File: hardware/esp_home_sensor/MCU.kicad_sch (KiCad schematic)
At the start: 9 parts, among them SW1 SW_Push, SW2 SW_Push, U6 ESP32-C6-MINI-1

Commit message: busses, display connector, footprint lib
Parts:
- added C15, C16: C, symbol Device:C
- added SW3: SW_Push, symbol Switch:SW_Push
- D3: footprint LED_SMD:LED_WS2812B_PLCC4_5.0x5.0mm_P3.2mm -> LED_SMD:LED_WS2812B-2020_PLCC4_2.0x2.0mm
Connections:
- net 3V3_EN: now also U6.13 (IO1); no longer U6.26 (IO20)
- net ADC_BAT: now also U6.5 (IO2); no longer U6.28 (IO22)
- net BOOT: now also C16.1
- net GND: now also C15.2, C16.2, SW3.1
- net LED_DATA: now also U6.12 (IO0); no longer U6.27 (IO21)
- net USER_SW: now also C15.1, SW3.2
- net I2C.SDA: now reaches U6.19 (IO14)
- net I2C.SCL: now reaches U6.20 (IO15)
- net DISP_IF.RST: now reaches U6.29 (IO23)
- net SCL renamed DISP_IF.MOSI
- net SDA renamed DISP_IF.CLK
- net USB_N renamed USB.USB_N
- net USB_P renamed USB.USB_P
- new net DISP_IF.BUSY: U6.28 (IO22)
- new net DISP_IF.CS: U6.26 (IO20)
- new net DISP_IF.DC: U6.27 (IO21)
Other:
- moved on the sheet: SW2

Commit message: footprint assignment, buck
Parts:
- C12, C13: value C -> 4.7u; footprint (none) -> Capacitor_SMD:C_0402_1005Metric
- C15, C16: value C -> 100n; footprint (none) -> Capacitor_SMD:C_0402_1005Metric
- C9: value C -> 1u; footprint (none) -> Capacitor_SMD:C_0402_1005Metric
- R12: value R -> 100k; footprint (none) -> Resistor_SMD:R_0402_1005Metric
- SW1, SW2, SW3: Mfr. No. (none) -> B3FS-1010P
- U6: Mfr. No. (none) -> ESP32-C6-MINI-1U-N4
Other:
- moved on the sheet: C15, C16, C9, R12, SW1, SW2, SW3

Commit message: minor update
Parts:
- JP2: footprint (none) -> Jumper:SolderJumper-3_P1.3mm_Bridged12_Pad1.0x1.5mm
- SW1, SW2, SW3: footprint (none) -> Button_Switch_SMD:SW_SPST_Omron_B3FS-101xP
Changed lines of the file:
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@@
 			)
 		)
-		(property "Footprint" ""
+		(property "Footprint" "Jumper:SolderJumper-3_P1.3mm_Bridged12_Pad1.0x1.5mm"
 			(at 232.41 95.25 0)
 			(hide yes)
@@
 			)
 		)
-		(property "Footprint" ""
+		(property "Footprint" "Button_Switch_SMD:SW_SPST_Omron_B3FS-101xP"
 			(at 99.06 119.38 0)
 			(hide yes)
@@
 			)
 		)
-		(property "Footprint" ""
+		(property "Footprint" "Button_Switch_SMD:SW_SPST_Omron_B3FS-101xP"
 			(at 71.12 90.17 0)
 			(hide yes)
@@
 			)
 		)
-		(property "Footprint" ""
+		(property "Footprint" "Button_Switch_SMD:SW_SPST_Omron_B3FS-101xP"
 			(at 71.12 119.38 0)
 			(hide yes)

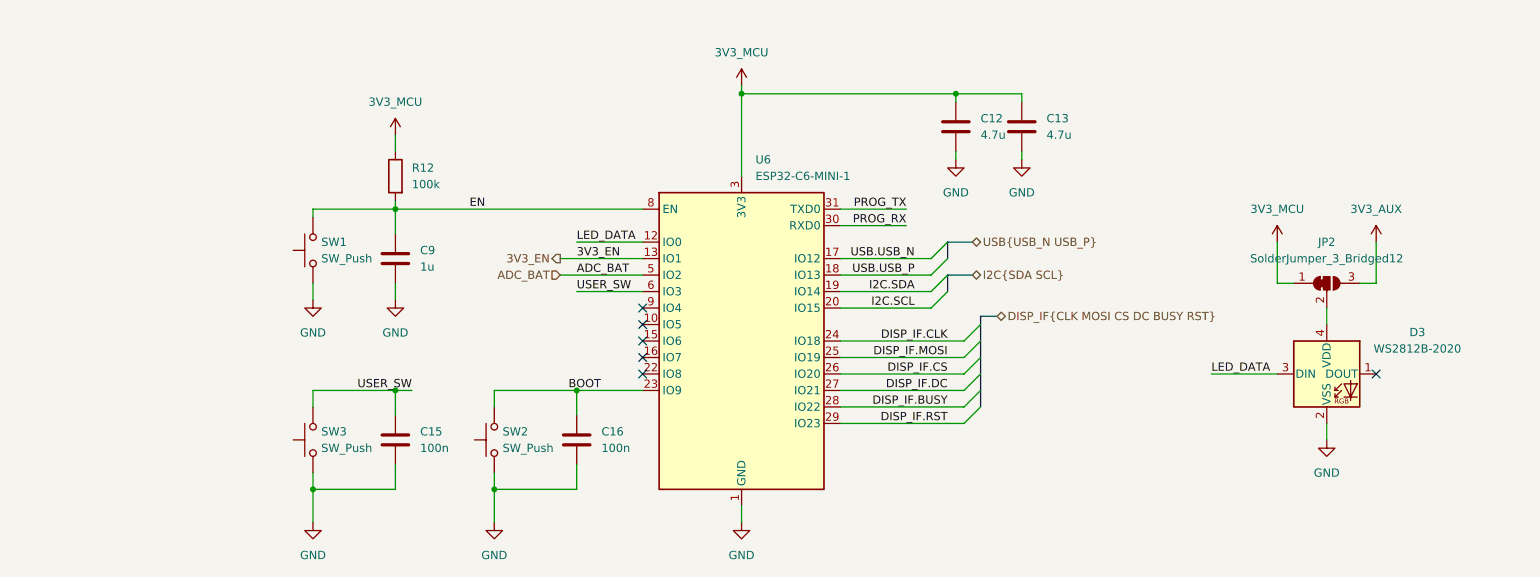
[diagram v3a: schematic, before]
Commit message: initial layout, power routing
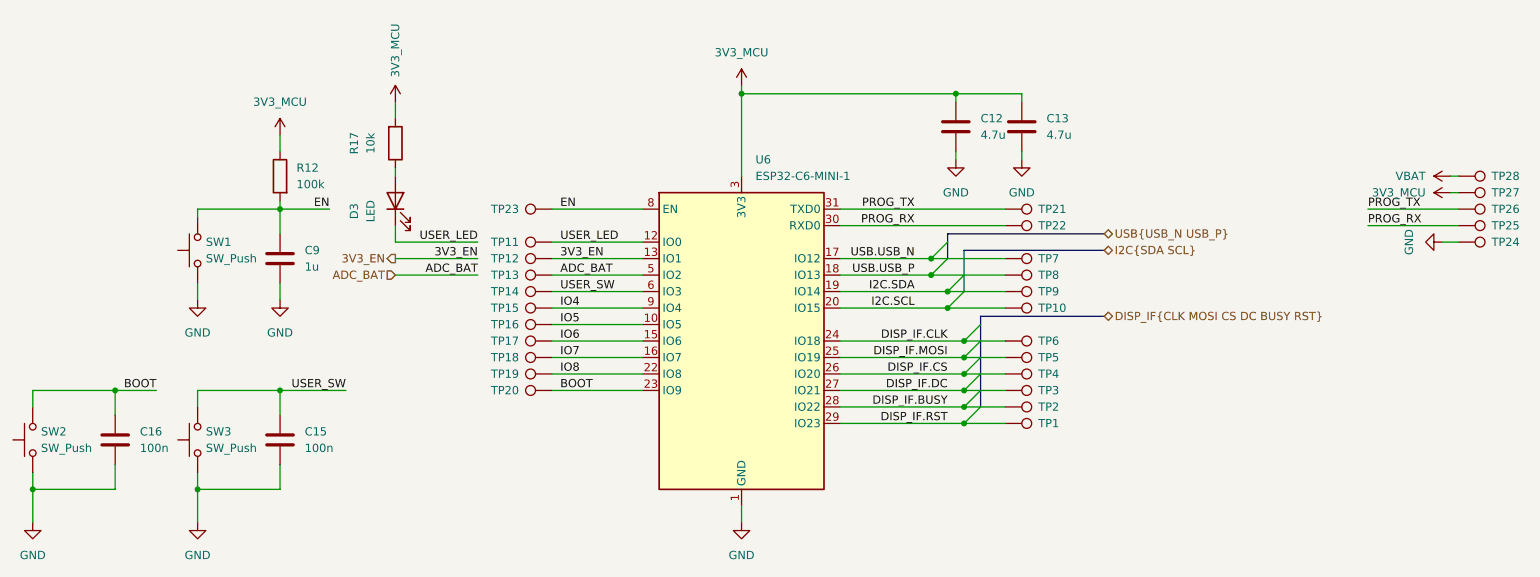
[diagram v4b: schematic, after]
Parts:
- removed D3: WS2812B-2020, LED_SMD:LED_WS2812B-2020_PLCC4_2.0x2.0mm, symbol LED:WS2812B-2020
- removed JP2: SolderJumper_3_Bridged12, Jumper:SolderJumper-3_P1.3mm_Bridged12_Pad1.0x1.5mm, symbol Jumper:SolderJumper_3_Bridged12
- added D3: LED, LED_SMD:LED_0402_1005Metric, symbol Device:LED
- added R17: 10k, Resistor_SMD:R_0402_1005Metric, symbol Device:R
- added TP1, TP10, TP11, TP12, TP13, TP14, TP15, TP16, TP17, TP18, TP19, TP2, TP20, TP21, TP22, TP23, TP3, TP4, TP5, TP6, TP7, TP8, TP9: TestPoint, TestPoint:TestPoint_Pad_D1.0mm, symbol Connector:TestPoint
- added TP24, TP25, TP26, TP27, TP28: TestPoint, TestPoint:TestPoint_Pad_D2.5mm, symbol Connector:TestPoint
- SW1, SW3: footprint Button_Switch_SMD:SW_SPST_Omron_B3FS-101xP -> Button_Switch_SMD:SW_Push_1P1T_NO_CK_KMR2; Mfr. No. B3FS-1010P -> (none)
- SW2: footprint Button_Switch_SMD:SW_SPST_Omron_B3FS-101xP -> Button_Switch_SMD:SW_Push_1P1T_NO_CK_KMR2; Mfr. No. B3FS-1010P -> KMR232NG ULC LFS
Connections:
- net 3V3_EN: now also TP12.1
- net 3V3_MCU: now also R17.2, TP27.1
- net ADC_BAT: now also TP13.1
- net BOOT: now also TP20.1
- net DISP_IF.BUSY: now also TP2.1
- net DISP_IF.CLK: now also TP6.1
- net DISP_IF.CS: now also TP4.1
- net DISP_IF.DC: now also TP3.1
- net DISP_IF.MOSI: now also TP5.1
- net DISP_IF.RST: now also TP1.1
- net EN: now also TP23.1
- net GND: now also TP24.1
- net I2C.SCL: now also TP10.1
- net I2C.SDA: now also TP9.1
- net PROG_RX: now also TP22.1, TP25.1
- net PROG_TX: now also TP21.1, TP26.1
- net USB.USB_N: now also TP7.1
- net USB.USB_P: now also TP8.1
- net USER_SW: now also TP14.1
- net IO5: now reaches U6.10 (IO5)
- net IO5: now also TP16.1
- net IO6: now reaches U6.15 (IO6)
- net IO6: now also TP17.1
- net IO7: now reaches U6.16 (IO7)
- net IO7: now also TP18.1
- net IO8: now reaches U6.22 (IO8)
- net IO8: now also TP19.1
- net IO4: now reaches U6.9 (IO4)
- net IO4: now also TP15.1
- net LED_DATA renamed USER_LED
- net USER_LED: now also D3.1 (K), TP11.1
- new net: D3.2 (A), R17.1
- new net VBAT: TP28.1
- no-connect marks 6 -> 0
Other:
- moved on the sheet: C15, C9, R12, SW1, SW3

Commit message: layout
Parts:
- removed TP24, TP25, TP26, TP27, TP28: TestPoint, TestPoint:TestPoint_Pad_D2.5mm, symbol Connector:TestPoint

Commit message: layout
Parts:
- renumbered C9 to C10, C15 to C11, C16 to C9, R12 to R15, R17 to R16, SW2 to SW1, SW1 to SW2, TP13 to TP10, TP14 to TP11, TP15 to TP12, TP16 to TP13, TP17 to TP14, TP18 to TP15, TP19 to TP16, TP20 to TP17, TP21 to TP18, TP22 to TP19, TP7 to TP20, TP8 to TP21, TP9 to TP22, TP10 to TP23, TP6 to TP24, TP5 to TP25, TP4 to TP26, TP3 to TP27, TP2 to TP28, TP1 to TP29, TP23 to TP7, TP11 to TP8, TP12 to TP9

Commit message: in production
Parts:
- C10: Mfr. No. (none) -> GRM155R61E105MA12D
- C11, C9: Mfr. No. (none) -> GRM155R71H104KE14D
- C12, C13: Mfr. No. (none) -> GRM155C61E475ME15D
- D3: Mfr. No. (none) -> LTST-C281KRKT
- R15: Mfr. No. (none) -> RC0402FR-07100KL
- R16: Mfr. No. (none) -> RC0402FR-0710KL
- SW1: Mfr. No. KMR232NG ULC LFS -> KMR232NG ULC LFS
- SW2, SW3: Mfr. No. (none) -> KMR232NG ULC LFS
- TP10, TP11, TP12, TP13, TP14, TP15, TP16, TP17, TP18, TP19, TP20, TP21, TP22, TP23, TP24, TP25, TP26, TP27, TP28, TP29, TP7, TP8, TP9: now left out of the parts list
- U6: Mfr. No. ESP32-C6-MINI-1U-N4 -> ESP32-C6-MINI-1U-N4
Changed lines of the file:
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@@
 			)
 		)
-		(property "Mfr. No." " ESP32-C6-MINI-1U-N4 "
+		(property "Mfr. No." " ESP32-C6-MINI-1U-N4"
 			(at 142.24 104.14 0)
 			(hide yes)
@@
 		(body_style 1)
 		(exclude_from_sim no)
-		(in_bom yes)
+		(in_bom no)
 		(on_board yes)
 		(in_pos_files yes)
@@
 		(body_style 1)
 		(exclude_from_sim no)
-		(in_bom yes)
+		(in_bom no)
 		(on_board yes)
 		(in_pos_files yes)
@@
 		(body_style 1)
 		(exclude_from_sim no)
-		(in_bom yes)
+		(in_bom no)
 		(on_board yes)
 		(in_pos_files yes)
@@
 			)
 		)
-		(property "Mfr. No." ""
+		(property "Mfr. No." "RC0402FR-0710KL"
 			(at 88.9 73.66 90)
 			(hide yes)
@@
 		(body_style 1)
 		(exclude_from_sim no)
-		(in_bom yes)
+		(in_bom no)
 		(on_board yes)
 		(in_pos_files yes)
@@
 		(body_style 1)
 		(exclude_from_sim no)
-		(in_bom yes)
+		(in_bom no)
 		(on_board yes)
 		(in_pos_files yes)
@@
 			)
 		)
-		(property "Mfr. No." "KMR232NG ULC LFS "
+		(property "Mfr. No." "KMR232NG ULC LFS"
 			(at 33.02 119.38 90)
 			(hide yes)
@@
 		(body_style 1)
 		(exclude_from_sim no)
-		(in_bom yes)
+		(in_bom no)
 		(on_board yes)
 		(in_pos_files yes)
@@
 			)
 		)
-		(property "Mfr. No." ""
+		(property "Mfr. No." "GRM155R71H104KE14D"
 			(at 45.72 119.38 0)
 			(hide yes)
@@
 		(body_style 1)
 		(exclude_from_sim no)
-		(in_bom yes)
+		(in_bom no)
 		(on_board yes)
 		(in_pos_files yes)
@@
 			)
 		)
-		(property "Mfr. No." ""
+		(property "Mfr. No." "KMR232NG ULC LFS"
 			(at 58.42 90.17 90)
 			(hide yes)
@@
 		(body_style 1)
 		(exclude_from_sim no)
-		(in_bom yes)
+		(in_bom no)
 		(on_board yes)
 		(in_pos_files yes)
@@
 		(body_style 1)
 		(exclude_from_sim no)
-		(in_bom yes)
+		(in_bom no)
 		(on_board yes)
 		(in_pos_files yes)
@@
 		(body_style 1)
 		(exclude_from_sim no)
-		(in_bom yes)
+		(in_bom no)
 		(on_board yes)
 		(in_pos_files yes)
@@
 		(body_style 1)
 		(exclude_from_sim no)
-		(in_bom yes)
+		(in_bom no)
 		(on_board yes)
 		(in_pos_files yes)
@@
 		(body_style 1)
 		(exclude_from_sim no)
-		(in_bom yes)
+		(in_bom no)
 		(on_board yes)
 		(in_pos_files yes)
@@
 		(body_style 1)
 		(exclude_from_sim no)
-		(in_bom yes)
+		(in_bom no)
 		(on_board yes)
 		(in_pos_files yes)
@@
 			)
 		)
-		(property "Mfr. No." ""
+		(property "Mfr. No." "RC0402FR-07100KL"
 			(at 71.12 78.74 0)
 			(hide yes)
@@
 		(body_style 1)
 		(exclude_from_sim no)
-		(in_bom yes)
+		(in_bom no)
 		(on_board yes)
 		(in_pos_files yes)
@@
 		(body_style 1)
 		(exclude_from_sim no)
-		(in_bom yes)
+		(in_bom no)
 		(on_board yes)
 		(in_pos_files yes)
@@
 			)
 		)
-		(property "Mfr. No." ""
+		(property "Mfr. No." "LTST-C281KRKT"
 			(at 88.9 82.55 0)
 			(hide yes)
@@
 			)
 		)
-		(property "Mfr. No." ""
+		(property "Mfr. No." "GRM155C61E475ME15D"
 			(at 185.42 71.12 0)
 			(hide yes)
@@
 		(body_style 1)
 		(exclude_from_sim no)
-		(in_bom yes)
+		(in_bom no)
 		(on_board yes)
 		(in_pos_files yes)
@@
 		(body_style 1)
 		(exclude_from_sim no)
-		(in_bom yes)
+		(in_bom no)
 		(on_board yes)
 		(in_pos_files yes)
@@
 			)
 		)
-		(property "Mfr. No." ""
+		(property "Mfr. No." "KMR232NG ULC LFS"
 			(at 58.42 119.38 90)
 			(hide yes)
@@
 		(body_style 1)
 		(exclude_from_sim no)
-		(in_bom yes)
+		(in_bom no)
 		(on_board yes)
 		(in_pos_files yes)
@@
 			)
 		)
-		(property "Mfr. No." ""
+		(property "Mfr. No." "GRM155R71H104KE14D"
 			(at 71.12 119.38 0)
 			(hide yes)
@@
 		(body_style 1)
 		(exclude_from_sim no)
-		(in_bom yes)
+		(in_bom no)
 		(on_board yes)
 		(in_pos_files yes)
@@
 		(body_style 1)
 		(exclude_from_sim no)
-		(in_bom yes)
+		(in_bom no)
 		(on_board yes)
 		(in_pos_files yes)
@@
 		(body_style 1)
 		(exclude_from_sim no)
-		(in_bom yes)
+		(in_bom no)
 		(on_board yes)
 		(in_pos_files yes)
@@
 		(body_style 1)
 		(exclude_from_sim no)
-		(in_bom yes)
+		(in_bom no)
 		(on_board yes)
 		(in_pos_files yes)
@@
 			)
 		)
-		(property "Mfr. No." ""
+		(property "Mfr. No." "GRM155R61E105MA12D"
 			(at 71.12 91.44 0)
 			(hide yes)
@@
 		(body_style 1)
 		(exclude_from_sim no)
-		(in_bom yes)
+		(in_bom no)
 		(on_board yes)
 		(in_pos_files yes)
@@
 			)
 		)
-		(property "Mfr. No." ""
+		(property "Mfr. No." "GRM155C61E475ME15D"
 			(at 175.26 71.12 0)
 			(hide yes)

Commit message: az
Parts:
- U6: Down_current (none) -> 7u; Supply_current (none) -> 500m
